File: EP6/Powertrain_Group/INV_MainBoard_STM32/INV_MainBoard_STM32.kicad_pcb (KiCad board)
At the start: 4 copper layers, 100 x 92 mm, 249 parts, among them J1 FX26-30P-1SV, J10 current_DC, J11 current_U, J12 current_V, J13 current_W, J2 motorSense, J3 LVBattery, J4 STDC14, J5 current_DC, J6 current_U, J7 current_V, J8 current_V, J9 CAN, SW1 RESET, U1 OPA340NA, U10 OPA340NA, U11 OPA340NA, U12 OPA340NA, U13 LMV7219M5, U14 LMV7219M5, U15 LMV7219M5, U16 LMV7219M5, U17 LMV7219M5, U18 LMV7219M5, U19 LMV7219M5, U2 TPS5430DDA, U20 LMV7219M5, U21 OPA340NA, U22 TCAN1042VDRQ1, U3 AMS1117-3.3, U4 STM32G474RETx, U5 CAT24C256, U6 TCAN1042VDRQ1, U7 OPA340NA, U8 OPA340NA, U9 OPA340NA, Y1 Crystal_GND23

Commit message: Inverter board adjust
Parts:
- D3, D5: footprint Diode_SMD:D_SMB -> Diode_SMD:D_SOD-323
- R4: footprint Resistor_SMD:R_0402_1005Metric -> Resistor_SMD:R_0603_1608Metric
- U2: value TPS5430DDA -> TPS5430DDAR
- moved R10 25.8 mm to (183.0, 50.2), turned to 0 degrees
- moved D5 24.1 mm to (184.8, 64.8), turned to -90 degrees
- moved C15 23.6 mm to (179.0, 63.0), turned to 90 degrees
- moved C12 23.6 mm to (178.2, 68.8), turned to -90 degrees
- moved F2 22.5 mm to (181.2, 54.5), turned to 0 degrees
- moved TP3 22.2 mm to (178.8, 47.5), turned to 90 degrees
- moved D6 21.3 mm to (179.6, 50.1), turned to 180 degrees
- moved C13 20.6 mm to (175.8, 68.8), turned to -90 degrees
- moved C14 17.8 mm to (164.8, 68.5), turned to 180 degrees
- moved R9 5.89 mm to (156.2, 42.2), turned to 180 degrees
- moved R8 5.40 mm to (160.2, 42.2)
- moved FB1 4.77 mm to (246.5, 93.8), turned to -90 degrees
- moved C20 3.02 mm to (183.2, 68.0), turned to 0 degrees
- moved L3 2.85 mm to (167.2, 60.0), turned to 0 degrees
- moved C9 2.84 mm to (157.5, 58.0)
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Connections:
- J1 pad MP1: GND -> unconnected-(J1-PadMP1)
- J1 pad MP2: GND -> unconnected-(J1-PadMP2)
- J1 pad MP3: GND -> unconnected-(J1-PadMP3)
- J1 pad MP4: GND -> unconnected-(J1-PadMP4)
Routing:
- net +5V: track 357.9 -> 288.1 mm, vias 4 -> 3
- net /Power/5V_buck: track 51.9 -> 63.8 mm
- net GND: track 218.8 -> 228.6 mm, vias 104 -> 87
- net /EncoderDifVconverter/Vref_1.65V: track 8.27 -> 16.6 mm
- net +3V3: track 77.8 -> 71.1 mm, vias 72 -> 67
- net +24V: track 228.0 -> 234.1 mm
- net /Power/5V_buck_sw: track 17.2 -> 12.3 mm
- net /Power/5V_buck_FB: track 3.43 -> 7.02 mm
- net /GATE_EN: track 131.0 -> 128.1 mm, vias 8 -> 6
- net /FLTN: track 40.7 -> 42.8 mm, vias 2 -> 1
- net /MCU/CrystalGND: track 17.8 -> 19.5 mm, vias 13 -> 14
- net /Isense_OCP/+24V_4-20mA: track 15.0 -> 16.5 mm
- net /Power/+24V_proCMfilter: track 14.5 -> 15.5 mm
- net Net-(J13-Pin_1): track 5.12 -> 6.12 mm
- net Net-(J13-Pin_2): track 4.27 -> 5.27 mm
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- added copper zone on B.Cu, net GND
- added copper zone on F.Cu, net GND

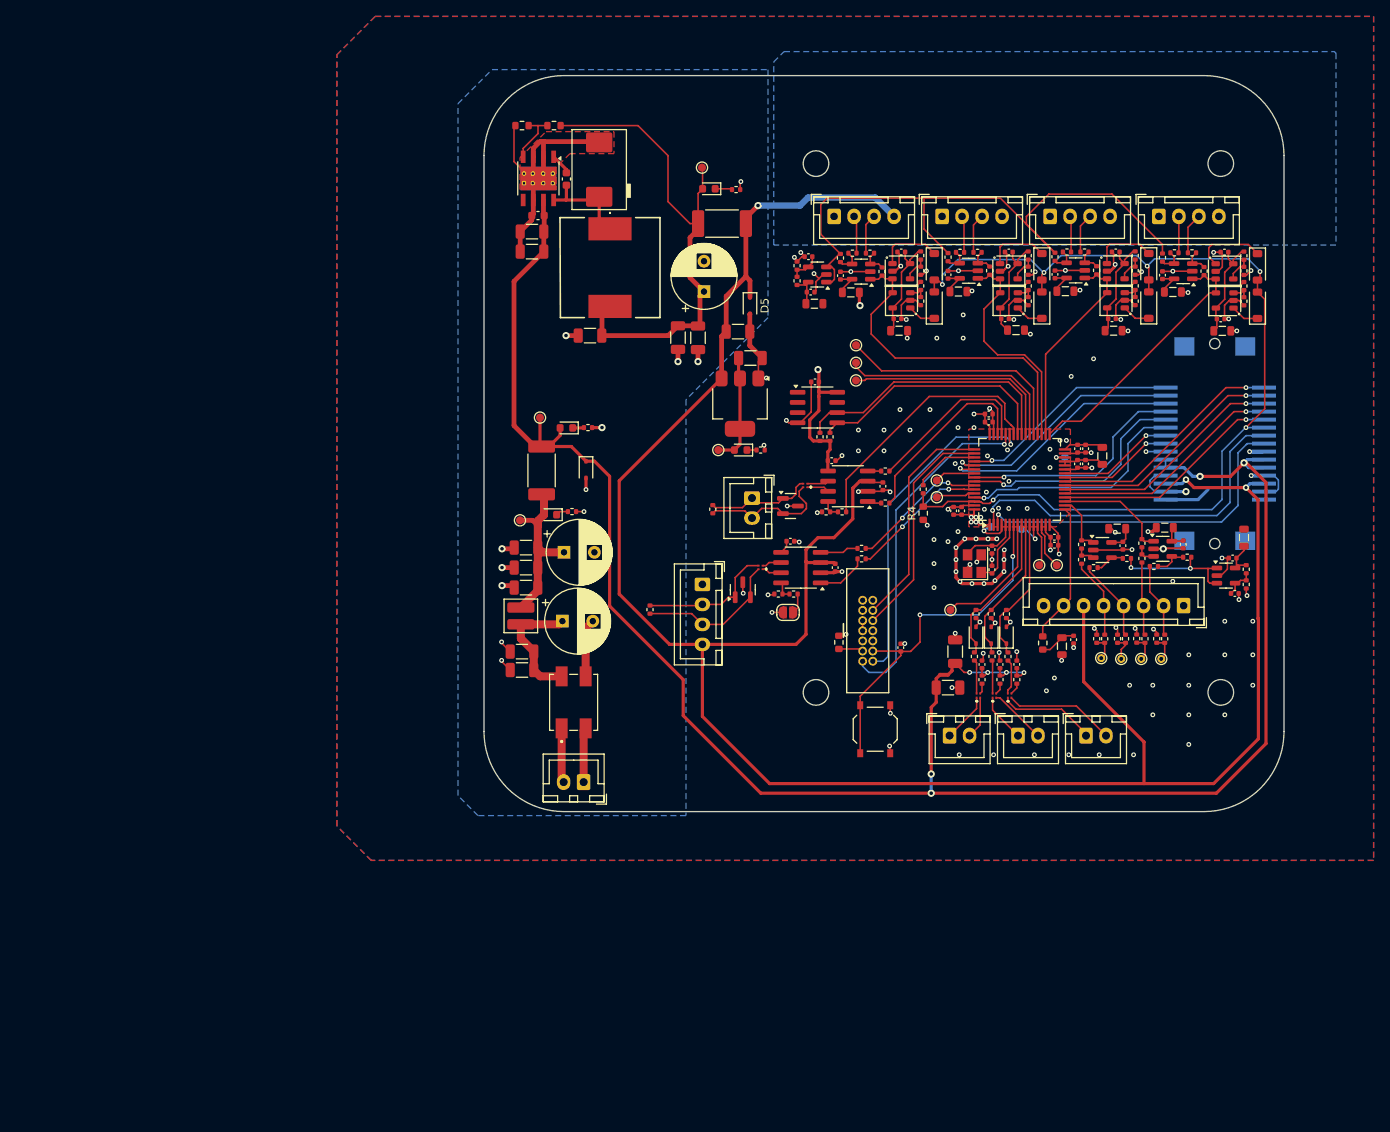
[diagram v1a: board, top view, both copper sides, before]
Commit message: batch update for JLCPCB 241117
6SBMS
ACC_HVLV1
INV_CurrentSense2
INV_CurrentSense3
DClinkCap1
INV_MainBoard_STM32
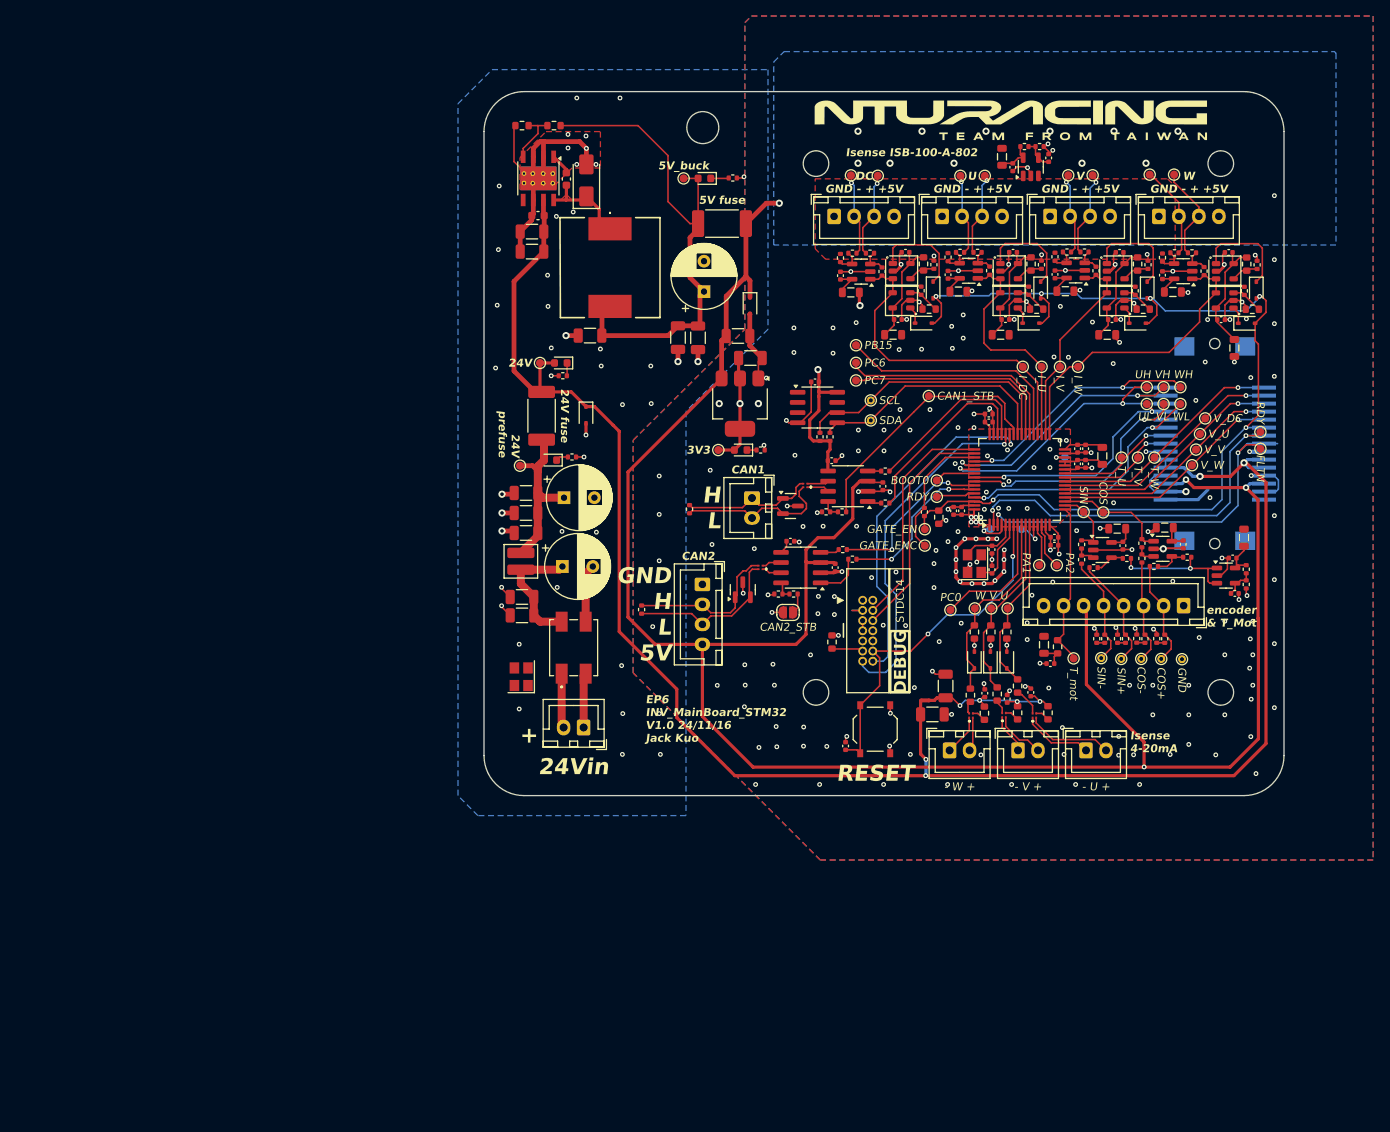
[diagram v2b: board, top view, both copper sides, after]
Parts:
- added H5: M4, MountingHole:MountingHole_4mm, F.Cu at (178.8, 42.5)
- added TP12: eCOS, TestPoint:TestPoint_Pad_D1.0mm, F.Cu at (228.9, 90.6)
- added TP21: eSIN, TestPoint:TestPoint_Pad_D1.0mm, F.Cu at (226.4, 90.5)
- added TP22: WH, TestPoint:TestPoint_Pad_D1.0mm, F.Cu at (238.6, 75.0)
- added TP23: VH, TestPoint:TestPoint_Pad_D1.0mm, F.Cu at (236.4, 75.0)
- added TP24: UH, TestPoint:TestPoint_Pad_D1.0mm, F.Cu at (234.3, 75.0)
- added TP25: Ready, TestPoint:TestPoint_Pad_D1.0mm, F.Cu at (248.6, 80.5)
- added TP26: NFLT, TestPoint:TestPoint_Pad_D1.0mm, F.Cu at (248.6, 82.7)
- added TP27: GEnC, TestPoint:TestPoint_Pad_D1.0mm, F.Cu at (206.6, 94.8)
- added TP28: CAN1_STB, TestPoint:TestPoint_Pad_D1.0mm, F.Cu at (207.1, 76.0)
- added TP29: TW, TestPoint:TestPoint_Pad_D1.0mm, F.Cu at (235.3, 83.8)
- added TP30: TV, TestPoint:TestPoint_Pad_D1.0mm, F.Cu at (233.2, 83.8)
- added TP31: TU, TestPoint:TestPoint_Pad_D1.0mm, F.Cu at (231.2, 83.8)
- added TP32: UL, TestPoint:TestPoint_Pad_D1.0mm, F.Cu at (234.3, 77.0)
- added TP33: VL, TestPoint:TestPoint_Pad_D1.0mm, F.Cu at (236.4, 77.0)
- added TP34: WL, TestPoint:TestPoint_Pad_D1.0mm, F.Cu at (238.6, 77.0)
- added TP35: GEnFb, TestPoint:TestPoint_Pad_D1.0mm, F.Cu at (206.6, 92.7)
- added TP36: IW, TestPoint:TestPoint_Pad_D1.0mm, F.Cu at (225.8, 72.4)
- added TP37: IV, TestPoint:TestPoint_Pad_D1.0mm, F.Cu at (223.5, 72.4)
- added TP38: IU, TestPoint:TestPoint_Pad_D1.0mm, F.Cu at (221.2, 72.4)
- added TP39: IDC, TestPoint:TestPoint_Pad_D1.0mm, F.Cu at (218.8, 72.4)
- added TP40: IcW, TestPoint:TestPoint_Pad_D1.0mm, F.Cu at (212.8, 102.6)
- added TP41: IcV, TestPoint:TestPoint_Pad_D1.0mm, F.Cu at (214.9, 102.6)
- added TP42: IcU, TestPoint:TestPoint_Pad_D1.0mm, F.Cu at (216.9, 102.6)
- added TP43: VU, TestPoint:TestPoint_Pad_D1.0mm, F.Cu at (241.0, 80.8)
- added TP44: VDC, TestPoint:TestPoint_Pad_D1.0mm, F.Cu at (241.7, 78.8)
- added TP45: VV, TestPoint:TestPoint_Pad_D1.0mm, F.Cu at (240.5, 82.8)
- added TP46: VW, TestPoint:TestPoint_Pad_D1.0mm, F.Cu at (240.0, 84.7)
- added TP47: TM, TestPoint:TestPoint_Pad_D1.0mm, F.Cu at (225.2, 108.8)
- added TP48: GND, TestPoint:TestPoint_THTPad_D1.0mm_Drill0.5mm, F.Cu at (238.8, 109.0)
- added TP49: SCL, TestPoint:TestPoint_THTPad_D1.0mm_Drill0.5mm, F.Cu at (199.8, 76.6)
- added TP50: SDA, TestPoint:TestPoint_THTPad_D1.0mm_Drill0.5mm, F.Cu at (199.8, 79.1)
- added TP51: I_DC+, TestPoint:TestPoint_Pad_D1.0mm, F.Cu at (200.7, 48.5)
- added TP52: I_DC-, TestPoint:TestPoint_Pad_D1.0mm, F.Cu at (197.4, 48.5)
- added TP53: I_U+, TestPoint:TestPoint_Pad_D1.0mm, F.Cu at (214.1, 48.5)
- added TP54: I_U-, TestPoint:TestPoint_Pad_D1.0mm, F.Cu at (211.1, 48.5)
- added TP55: I_V+, TestPoint:TestPoint_Pad_D1.0mm, F.Cu at (227.6, 48.5)
- added TP56: I_V-, TestPoint:TestPoint_Pad_D1.0mm, F.Cu at (224.5, 48.5)
- added TP57: I_W+, TestPoint:TestPoint_Pad_D1.0mm, F.Cu at (237.8, 48.4)
- added TP58: I_W-, TestPoint:TestPoint_Pad_D1.0mm, F.Cu at (234.7, 48.4)
- added Y2: X322516MLB4SI 16MHz, Crystal:Crystal_SMD_3225-4Pin_3.2x2.5mm, F.Cu at (156.2, 111.1)
- D10, D11, D12, D13, D14, D15, D16, D9: footprint Diode_SMD:D_SOD-123 -> Diode_SMD:D_SOD-323
- D18, D19, D20: value 3.7V -> 3.7V BZT52C3V9S
- D3: value zener 27V -> 27V BZT52C27
- D4: footprint PCM_Diode_SMD_AKL:D_SMC -> Diode_SMD:D_SMA
- D5: value zener 5.6V -> 5.6V BZT52C5V6S
- FB1, FB10, FB11, FB13, FB15, FB2, FB3, FB4, FB5, FB6, FB7, FB8, FB9: value GZ1608D601TF -> GZ2012D601TF
- R5: value 1k 1% -> 1k
- R52, R53, R56, R57, R60, R61, R64, R65, R75, R76, R77: footprint Resistor_SMD:R_0402_1005Metric -> Resistor_SMD:R_0603_1608Metric
- R78, R79, R80, R81, R82, R83: value 150R -> 100R; footprint Resistor_SMD:R_0402_1005Metric -> Resistor_SMD:R_0603_1608Metric
- SW1: value RESET -> TS-1187A-B-A-B
- TP5: value sin- -> sin+
- TP6: value sin+ -> sin-
- Y1: value Crystal_GND23 -> X322525MOB4SI 25Mhz
- moved R69 33.8 mm to (221.0, 44.9), turned to 0 degrees
- moved R68 33.0 mm to (219.1, 44.9), turned to 0 degrees
- moved C54 32.5 mm to (222.1, 46.3), turned to 90 degrees
- moved U21 29.9 mm to (219.8, 47.4), turned to 90 degrees
- moved FB10 29.8 mm to (216.2, 46.1), turned to -90 degrees
- moved C53 29.7 mm to (217.6, 47.5), turned to -90 degrees
- moved C32 14.1 mm to (196.7, 119.8)
- moved D2 8.15 mm to (161.1, 71.9)
- moved R7 7.20 mm to (161.3, 73.5), turned to 180 degrees
- moved C16 6.83 mm to (156.2, 101.2)
- moved C17 6.83 mm to (156.2, 103.5)
- moved C3 6.83 mm to (156.8, 88.2)
- moved C4 6.83 mm to (156.8, 90.7)
- moved C5 6.83 mm to (156.8, 93.2)
- moved C6 6.83 mm to (161.5, 88.8)
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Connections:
- TP5 pad 1: /EncoderDifVconverter/sin-3V3_out -> /SIN+
- TP6 pad 1: /EncoderDifVconverter/sin+3V3_out -> /SIN-
- TP7 pad 1: /EncoderDifVconverter/cos+3V3_out -> /COS+
- TP8 pad 1: /EncoderDifVconverter/cos-3V3_out -> /COS-
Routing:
- net /Isense_OCP/Vref_1.65V: track 81.6 -> 0.00 mm
- net +5V: track 288.1 -> 268.4 mm, vias 3 -> 4
- net +24V: track 234.1 -> 225.4 mm
- net /GATE_ENC: track 8.21 -> 16.6 mm
- net /WH: track 27.7 -> 35.6 mm, vias 1 -> 2
- net /Isense_OCP/IsenseNode3/IN-: track 4.57 -> 11.7 mm
- net /Isense_OCP/IsenseNode3/IN+: track 5.12 -> 11.9 mm
- net /Isense_OCP/IsenseNode2/IN+: track 4.95 -> 10.8 mm, vias 0 -> 1
- net /Isense_OCP/Isense_current_W: track 19.2 -> 25.1 mm
- net /Isense_OCP/IsenseNode2/IN-: track 4.50 -> 10.3 mm, vias 0 -> 1
- net /Isense_OCP/IsenseNode/IN-: track 4.73 -> 10.3 mm, vias 0 -> 1
- net /Isense_OCP/IsenseNode1/IN-: track 4.60 -> 10.2 mm, vias 0 -> 1
- net /Isense_OCP/IsenseNode/IN+: track 5.02 -> 10.6 mm, vias 0 -> 1
- net /Isense_OCP/IsenseNode1/IN+: track 4.94 -> 10.5 mm, vias 0 -> 1
- net /Isense_OCP/Isense_current_V: track 18.4 -> 23.6 mm
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- added copper zone on F.Cu, net /Isense_OCP/Vref_1.65V
- added copper zone on F.Cu, net /Power/5V_buck_sw
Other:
- board size 100 x 92 mm -> 100 x 88 mm
- board text added: "+"
- board text added: "- U +"
- board text added: "- V +"
- board text added: "- W +"
- board text added: "-3V3 -GND -5V -GND -24V -24V -GND -T_V -T_U -WL -VL -UL -UH -VH -WH"
- board text added: "24V"
- board text added: "24V fuse"
- board text added: "24V prefuse"
- board text added: "24Vin"
- board text added: "3V3"
- board text added: "3V3- GND- 5V- GND- 24V- 24V- GND- FLTN- GDY- GATE_EN- Vsense_W- Vsense_V- Vsense_U- Vsense_DC- T_W-"
- board text added: "5V fuse"
- board text added: "5V_buck"
- board text added: "BOOT0"
- board text added: "CAN1"
- board text added: "CAN1_STB"
- board text added: "CAN2"
- board text added: "CAN2_STB"
- board text added: "COS"
- board text added: "COS+"
- board text added: "COS-"
- board text added: "DC GND - + +5V"
- board text added: "DEBUG"
- board text added: "EP6 INV_MainBoard_STM32 V1.0 24/11/16 Jack Kuo"
- board text added: "FLTN"
- board text added: "FX26-30P-1SV"
- board text added: "GATE_EN"
- board text added: "GATE_ENC"
- board text added: "GND"
- board text added: "GND COS- COS+ COS- SIN- SIN+ +5V T_mot GND"
- board text added: "GND H L 5V"
- board text added: "H L"
- board text added: "I_DC"
- board text added: "I_U"
- board text added: "I_V"
- board text added: "I_W"
- board text added: "Isense 4-20mA"
- board text added: "Isense ISB-100-A-802"
- board text added: "PA0"
- board text added: "PA1"
- board text added: "PA2"
- board text added: "PB10"
- board text added: "PB15"
- board text added: "PC0"
- board text added: "PC15"
- board text added: "PC6"
- board text added: "PC7"
- board text added: "RDY"
- board text added: "RESET"
- board text added: "SCL"
- board text added: "SDA"
- board text added: "SIN"
- board text added: "SIN+"
- board text added: "SIN-"
- board text added: "STDC14"
- board text added: "T_U"
- board text added: "T_V"
- board text added: "T_W"
- board text added: "T_mot"
- board text added: "U GND - + +5V"
- board text added: "UH VH WH"
- board text added: "UL VL WL"
- board text added: "V GND - + +5V"
- board text added: "V_DC"
- board text added: "V_U"
- board text added: "V_V"
- board text added: "V_W"
- board text added: "W GND - + +5V"
- board text added: "W V U"
- board text added: "encoder & T_Mot"
